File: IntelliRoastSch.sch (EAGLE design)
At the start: 0 parts

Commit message: Added copies of MAX31855
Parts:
- added C1, C2, C4, C5, C7, C8: 10uF, adafruit:C-USC0805K
- added C3, C6, C9: 0.01µF, microbuilder:CAP_CERAMIC_0805
- added D1, D3, D5: 1n4148, adafruit:DIODESOD-323F
- added D2, D4, D6: 1N4148, adafruit:DIODESOD-323F
- added FB1, FB2, FB3, FB4, FB5, FB6: Ferrite, microbuilder:FERRITE_0805
- added IC1, IC3, IC5: MAX31855, adafruit:MAX6675
- added IC2, IC4, IC6: LP298XS, adafruit:LP298XS
- added J1, J2, J3: 1X2-3.5MM, adafruit:1X2-3.5MM
- added JP1, JP2, JP3: Breakout, microbuilder:HEADER-1X676MIL
- added R1, R2, R3, R4, R5, R6: 10K, adafruit:R-US_R0805
- added U$1, U$10, U$2, U$3, U$6, U$9: FIDUCIAL, adafruit:FIDUCIAL
- added U$11, U$12, U$4, U$5, U$7, U$8: MOUNTINGHOLE2.0, microbuilder:MOUNTINGHOLE2.0
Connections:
- new net +3V3: C1.1, C2.1, C4.1, C5.1, C7.1, C8.1, IC1.VCC, IC2.VOUT, IC3.VCC, IC4.VOUT, IC5.VCC, IC6.VOUT, JP1.2, JP2.2, JP3.2, R1.1, R2.1, R3.1, R4.1, R5.1, R6.1
- new net +5V: IC2.EN, IC2.VIN, IC4.EN, IC4.VIN, IC6.EN, IC6.VIN, JP1.1, JP2.1, JP3.1
- new net CS: D2.A, IC1./CS, R2.2
- new net CS1: D4.A, IC3./CS, R4.2
- new net CS2: D6.A, IC5./CS, R6.2
- new net DO: IC1.DO, JP1.4
- new net DO1: IC3.DO, JP2.4
- new net DO2: IC5.DO, JP3.4
- new net GND: C1.2, C2.2, C4.2, C5.2, C7.2, C8.2, IC1.GND, IC2.GND, IC3.GND, IC4.GND, IC5.GND, IC6.GND, JP1.3, JP2.3, JP3.3
- new net N$1: FB1.P$1, J1.2
- new net N$10: C6.P$1, FB3.P$2, IC3.T-
- new net N$11: FB4.P$1, J2.1
- new net N$12: C6.P$2, FB4.P$2, IC3.T+
- new net N$13: D6.C, JP3.5
- new net N$14: D5.C, JP3.6
- new net N$15: FB5.P$1, J3.2
- new net N$16: C9.P$1, FB5.P$2, IC5.T-
- new net N$17: FB6.P$1, J3.1
- new net N$18: C9.P$2, FB6.P$2, IC5.T+
- new net N$2: D2.C, JP1.5
- new net N$3: D1.C, JP1.6
- new net N$4: C3.P$1, FB1.P$2, IC1.T-
- new net N$5: FB2.P$1, J1.1
- new net N$6: C3.P$2, FB2.P$2, IC1.T+
- new net N$7: D4.C, JP2.5
- new net N$8: D3.C, JP2.6
- new net N$9: FB3.P$1, J2.2
- new net SCK: D1.A, IC1.SCK, R1.2
- new net SCK1: D3.A, IC3.SCK, R3.2
- new net SCK2: D5.A, IC5.SCK, R5.2

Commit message: Added MAX3221 chip
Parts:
- removed U$1, U$10, U$2, U$3, U$6, U$9: FIDUCIAL, adafruit:FIDUCIAL
- removed U$11, U$12, U$4, U$5, U$7, U$8: MOUNTINGHOLE2.0, microbuilder:MOUNTINGHOLE2.0
- added -TSSOP1: MAX3221-TSSOP16, MAX3221:MAX3221-TSSOP16
- added C10, C11, C12, C13, C14: 0.1uF, eagle-ltspice:CC0603
- added R7: 470, rcl:R-US_R0603
- added U1: STM32F2XXZXT, stm32f207zg:STM32F2XXZXT
- added U2: MOUDLE-BLUETOOTH-HC-05(34P-27X13MM), MOUDLE-BLUETOOTH-HC-05_34P-27X13MM_:MOUDLE-BLUETOOTH-HC-05(34P-27X13MM)
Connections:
- new net BT_UART_RX: -TSSOP1.DOUT, U2.UART-RX
- new net BT_UART_TX: -TSSOP1.RIN, U2.UART-TX
- new net C1+: -TSSOP1.C1+, C12.1
- new net C1-: -TSSOP1.C1-, C12.2
- new net C2+: -TSSOP1.C2+, C13.1
- new net C2-: -TSSOP1.C2-, C13.2
- new net N$19: R7.1, U2.PIO[9]
- new net N$21: -TSSOP1.V+, C10.1
- new net N$22: -TSSOP1.V-, C11.1
- new net STM_RX: -TSSOP1.ROUT
- new net STM_TX: -TSSOP1.DIN
- net +3V3: now also -TSSOP1.FORCEON, -TSSOP1.VCC, -TSSOP1.\!FORCEOFF, C14.2, U2.3.3V
- net GND: now also -TSSOP1.GND, -TSSOP1.\!EN, C10.2, C11.2, C14.1, U2.GND0, U2.GND1, U2.GND2, U2.GND3

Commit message: Updated with pin labels
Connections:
- new net BT_RX: U1A.PA3
- new net BT_TX: U1B.PD5
- new net LD2(BLUE): U1B.PB7
- new net LD3(RED): U1B.PB14
- new net MCO: U1A.PH0/OSC_IN
- new net RCC_OSC32_IN: U1A.PC14/OSC32_IN
- new net RCC_OSC32_OUT: U1A.PC15-OSC32_OUT
- new net RCC_OSC_OUT: U1A.PH1/OSC_OUT
- new net SPI1_MISO: U1A.PA6
- new net SPI1_MOSI: U1B.PB5
- new net SPI1_SCK: U1A.PA5
- new net SPI2_CS0: U1A.PF13
- new net SPI2_CS1: U1A.PE9
- new net STLK_RX: U1B.PD8
- new net STLK_TX: U1B.PD9
- new net TCK: U1B.PA14
- new net TIM2_CH1: U1A.PA0-WKUP
- new net TIM3_CH1: U1B.PC6
- new net TIM4_CH1: U1B.PD12
- new net TMS: U1B.PA13
- new net USB_OVERCURRENT: U1B.PG7
- new net USB_POWERSWITCHON: U1B.PG6
- new net USER_BTN(B1): U1A.PC13
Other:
- moved on the sheet: U1B

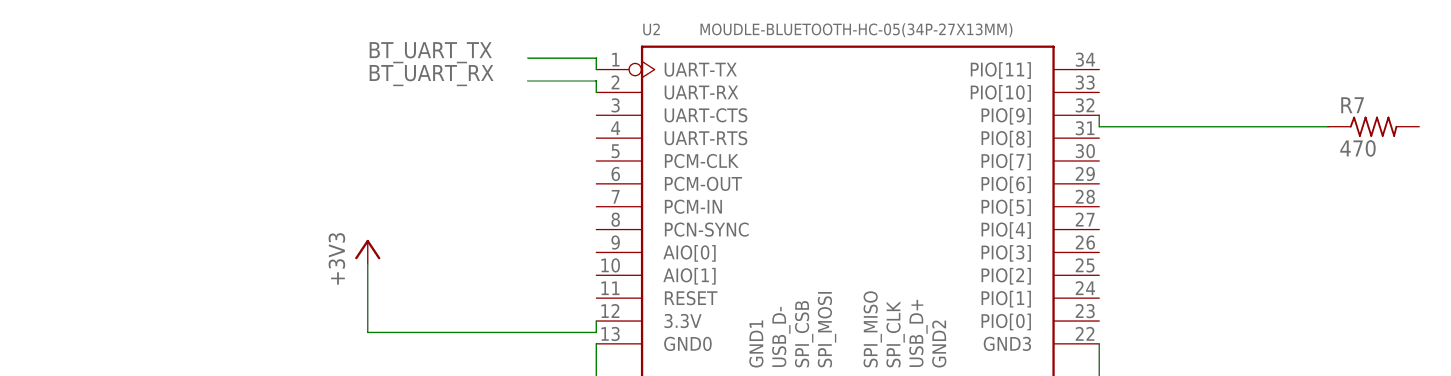
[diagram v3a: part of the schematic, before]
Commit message: Added zero Ohm resistors to RX and TX lines incase we're dumb and got it backwards
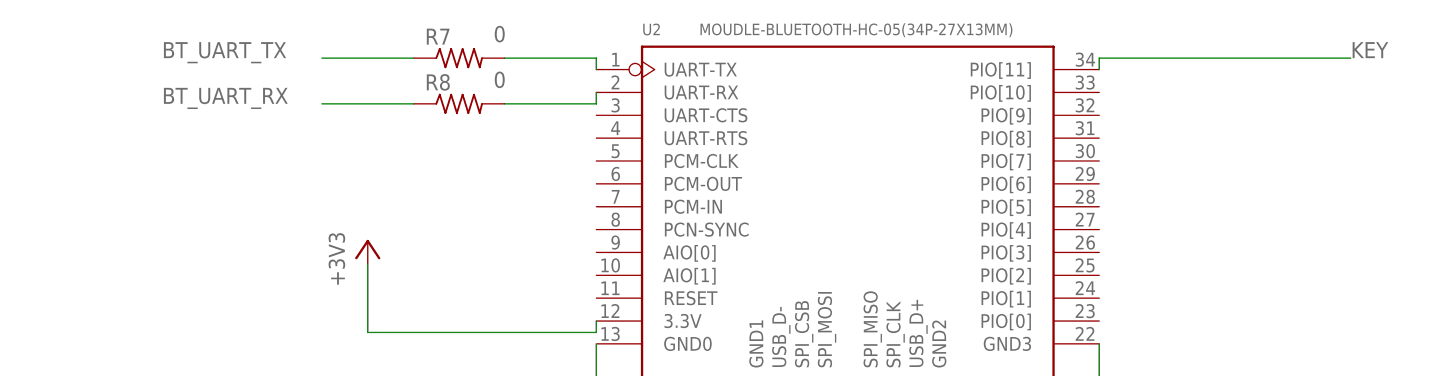
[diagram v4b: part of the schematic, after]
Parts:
- added R8: 0, adafruit:R-US_R0805
- R7: value 470 -> 0; device rcl:R-US_R0603 -> adafruit:R-US_R0805
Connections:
- removed net N$19: R7.1, U2.PIO[9]
- new net KEY: U2.PIO[11]
- new net N$23: R7.2, U2.UART-TX
- new net N$24: R8.2, U2.UART-RX
- net BT_UART_RX: now also R8.1; no longer U2.UART-RX
- net BT_UART_TX: now also R7.1; no longer U2.UART-TX
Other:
- moved on the sheet: R7
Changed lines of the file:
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@@
 <part name="+3V25" library="supply1" library_urn="urn:adsk.eagle:library:371" deviceset="+3V3" device=""/>
 <part name="GND16" library="supply1" library_urn="urn:adsk.eagle:library:371" deviceset="GND" device=""/>
-<part name="R7" library="rcl" library_urn="urn:adsk.eagle:library:334" deviceset="R-US_" device="R0603" package3d_urn="urn:adsk.eagle:package:23555/2" value="470"/>
 <part name="-TSSOP1" library="MAX3221" deviceset="MAX3221" device="-TSSOP16"/>
 <part name="GND17" library="supply1" library_urn="urn:adsk.eagle:library:371" deviceset="GND" device=""/>
@@
 <part name="C13" library="eagle-ltspice" library_urn="urn:adsk.eagle:library:217" deviceset="C" device="C0603" package3d_urn="urn:adsk.eagle:package:13262/1" value="0.1uF"/>
 <part name="C14" library="eagle-ltspice" library_urn="urn:adsk.eagle:library:217" deviceset="C" device="C0603" package3d_urn="urn:adsk.eagle:package:13262/1" value="0.1uF"/>
+<part name="R7" library="adafruit" deviceset="R-US_" device="R0805" value="0"/>
+<part name="R8" library="adafruit" deviceset="R-US_" device="R0805" value="0"/>
 </parts>
 <sheets>
@@
 <attribute name="VALUE" x="198.12" y="71.12" size="1.778" layer="96"/>
 </instance>
-<instance part="R7" gate="G$1" x="287.02" y="127" smashed="yes">
-<attribute name="NAME" x="283.21" y="128.4986" size="1.778" layer="95"/>
-<attribute name="VALUE" x="283.21" y="123.698" size="1.778" layer="96"/>
-</instance>
 <instance part="-TSSOP1" gate="G$1" x="228.6" y="15.24" smashed="yes">
 <attribute name="VALUE" x="215.8808" y="33.0469" size="1.67893125" layer="96"/>
@@
 <attribute name="NAME" x="288.036" y="25.019" size="1.778" layer="95"/>
 <attribute name="VALUE" x="293.116" y="22.479" size="1.778" layer="96" rot="R180"/>
+</instance>
+<instance part="R7" gate="G$1" x="185.42" y="134.62" smashed="yes">
+<attribute name="NAME" x="181.61" y="136.1186" size="1.778" layer="95"/>
+<attribute name="VALUE" x="189.23" y="136.398" size="1.778" layer="96"/>
+</instance>
+<instance part="R8" gate="G$1" x="185.42" y="129.54" smashed="yes">
+<attribute name="NAME" x="181.61" y="131.0386" size="1.778" layer="95"/>
+<attribute name="VALUE" x="189.23" y="131.318" size="1.778" layer="96"/>
 </instance>
 </instances>
@@
 </segment>
 </net>
-<net name="N$19" class="0">
-<segment>
-<pinref part="U2" gate="BT" pin="PIO[9]"/>
-<wire x1="256.54" y1="128.27" x2="256.54" y2="127" width="0.1524" layer="91"/>
-<wire x1="256.54" y1="127" x2="281.94" y2="127" width="0.1524" layer="91"/>
-<pinref part="R7" gate="G$1" pin="1"/>
-</segment>
-</net>
 <net name="BT_UART_TX" class="0">
-<segment>
-<pinref part="U2" gate="BT" pin="UART-TX"/>
-<wire x1="200.66" y1="133.35" x2="200.66" y2="134.62" width="0.1524" layer="91"/>
-<wire x1="200.66" y1="134.62" x2="193.04" y2="134.62" width="0.1524" layer="91"/>
-<label x="175.26" y="134.62" size="1.778" layer="95"/>
-</segment>
 <segment>
 <pinref part="-TSSOP1" gate="G$1" pin="RIN"/>
@@
 <label x="198.12" y="10.16" size="1.778" layer="95"/>
 </segment>
+<segment>
+<pinref part="R7" gate="G$1" pin="1"/>
+<wire x1="180.34" y1="134.62" x2="170.18" y2="134.62" width="0.1524" layer="91"/>
+<label x="152.4" y="134.62" size="1.778" layer="95"/>
+</segment>
 </net>
 <net name="BT_UART_RX" class="0">
-<segment>
-<pinref part="U2" gate="BT" pin="UART-RX"/>
-<wire x1="200.66" y1="130.81" x2="200.66" y2="132.08" width="0.1524" layer="91"/>
-<wire x1="200.66" y1="132.08" x2="193.04" y2="132.08" width="0.1524" layer="91"/>
-<label x="175.26" y="132.08" size="1.778" layer="95"/>
-</segment>
 <segment>
 <pinref part="-TSSOP1" gate="G$1" pin="DOUT"/>
 <wire x1="243.84" y1="20.32" x2="248.92" y2="20.32" width="0.1524" layer="91"/>
 <label x="248.92" y="20.32" size="1.778" layer="95"/>
+</segment>
+<segment>
+<pinref part="R8" gate="G$1" pin="1"/>
+<wire x1="180.34" y1="129.54" x2="170.18" y2="129.54" width="0.1524" layer="91"/>
+<label x="152.4" y="129.54" size="1.778" layer="95"/>
 </segment>
 </net>
@@
 <wire x1="-256.54" y1="-71.12" x2="-269.24" y2="-71.12" width="0.1524" layer="91"/>
 <label x="-287.02" y="-71.12" size="1.778" layer="95"/>
+</segment>
+</net>
+<net name="KEY" class="0">
+<segment>
+<pinref part="U2" gate="BT" pin="PIO[11]"/>
+<wire x1="256.54" y1="133.35" x2="256.54" y2="134.62" width="0.1524" layer="91"/>
+<wire x1="256.54" y1="134.62" x2="284.48" y2="134.62" width="0.1524" layer="91"/>
+<label x="284.48" y="134.62" size="1.778" layer="95"/>
+</segment>
+</net>
+<net name="N$23" class="0">
+<segment>
+<pinref part="U2" gate="BT" pin="UART-TX"/>
+<wire x1="200.66" y1="133.35" x2="200.66" y2="134.62" width="0.1524" layer="91"/>
+<pinref part="R7" gate="G$1" pin="2"/>
+<wire x1="200.66" y1="134.62" x2="190.5" y2="134.62" width="0.1524" layer="91"/>
+</segment>
+</net>
+<net name="N$24" class="0">
+<segment>
+<pinref part="U2" gate="BT" pin="UART-RX"/>
+<wire x1="200.66" y1="130.81" x2="200.66" y2="129.54" width="0.1524" layer="91"/>
+<pinref part="R8" gate="G$1" pin="2"/>
+<wire x1="200.66" y1="129.54" x2="190.5" y2="129.54" width="0.1524" layer="91"/>
 </segment>
 </net>
@@
 packages will not be understood (or retained) with this version.
 </note>
-<note version="8.4" severity="warning">
-Since Version 8.4, EAGLE supports properties for SPICE simulation.
-Probes in schematics and SPICE mapping objects found in parts and library devices
-will not be understood with this version. Update EAGLE to the latest version
-for full support of SPICE simulation.
-</note>
 </compatibility>
